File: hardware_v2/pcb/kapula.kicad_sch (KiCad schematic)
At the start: 166 parts, among them J1 Conn_02x10_Odd_Even, J2 Conn_02x10_Odd_Even, J3 U.FL, J4 U.FL, J5 U.FL, J6 U.FL, Q1 AO3401A, Q1 BSS84, Q2 AO3400A, Q3 AO3400A, Q4 AO3400A, Q5 AO3401A, T1 BW21S7511A01TF, T2 BW21S7511A01TF, T3 BW21S7511A01TF, T4 BW21S7511A01TF, U1 TP4054, U2 DW01+G, U3 XC6206P332MR, U4 FM8002A, U5 EFR32FG14P233F256GM48-B, U6 TG2016SMN 38.4000M-MCGNNM3, U7 XA213-G4J, Y1 32768 Hz

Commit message: PCB: Change some RF matching footprints, improve silkscreen
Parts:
- C74, C82: footprint kapula:C_0402_to_0603_HandSolder -> Capacitor_SMD:C_0603_1608Metric_Pad1.08x0.95mm_HandSolder; LCSC C1523 -> C1588
- L71, L72, L74, L75: footprint kapula:L_0402_to_0603_HandSolder -> Inductor_SMD:L_0402_1005Metric_Pad0.77x0.64mm_HandSolder
- R44, R45, R46, R47: footprint kapula:R_0402_to_0603_HandSolder -> Resistor_SMD:R_0603_1608Metric_Pad0.98x0.95mm_HandSolder
- R78: footprint kapula:R_0402_to_0603_HandSolder -> Resistor_SMD:R_0603_1608Metric_Pad0.98x0.95mm_HandSolder; LCSC C17168 -> C21189
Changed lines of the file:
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@@
       (effects (font (size 1.27 1.27)))
     )
-    (property "Footprint" "kapula:L_0402_to_0603_HandSolder" (at 177.8 196.85 0)
+    (property "Footprint" "Inductor_SMD:L_0402_1005Metric_Pad0.77x0.64mm_HandSolder" (at 177.8 196.85 0)
       (effects (font (size 1.27 1.27)) hide)
     )
@@
       (effects (font (size 1.27 1.27)))
     )
-    (property "Footprint" "kapula:C_0402_to_0603_HandSolder" (at 246.38 209.2452 0)
+    (property "Footprint" "Capacitor_SMD:C_0603_1608Metric_Pad1.08x0.95mm_HandSolder" (at 246.38 209.2452 0)
       (effects (font (size 1.27 1.27)) hide)
     )
@@
       (effects (font (size 1.27 1.27)) hide)
     )
-    (property "LCSC" "C1523" (at 250.19 208.28 0)
+    (property "LCSC" "C1588" (at 250.19 208.28 0)
       (effects (font (size 1.27 1.27)) hide)
     )
@@
       (effects (font (size 1.27 1.27)))
     )
-    (property "Footprint" "kapula:L_0402_to_0603_HandSolder" (at 177.8 207.01 0)
+    (property "Footprint" "Inductor_SMD:L_0402_1005Metric_Pad0.77x0.64mm_HandSolder" (at 177.8 207.01 0)
       (effects (font (size 1.27 1.27)) hide)
     )
@@
       (effects (font (size 1.27 1.27)))
     )
-    (property "Footprint" "kapula:C_0402_to_0603_HandSolder" (at 293.37 213.0552 0)
+    (property "Footprint" "Capacitor_SMD:C_0603_1608Metric_Pad1.08x0.95mm_HandSolder" (at 293.37 213.0552 0)
       (effects (font (size 1.27 1.27)) hide)
     )
@@
       (effects (font (size 1.27 1.27)) hide)
     )
-    (property "LCSC" "C1523" (at 297.18 212.09 0)
+    (property "LCSC" "C1588" (at 297.18 212.09 0)
       (effects (font (size 1.27 1.27)) hide)
     )
@@
       (effects (font (size 1.27 1.27)))
     )
-    (property "Footprint" "kapula:R_0402_to_0603_HandSolder" (at 393.7 25.908 90)
+    (property "Footprint" "Resistor_SMD:R_0603_1608Metric_Pad0.98x0.95mm_HandSolder" (at 393.7 25.908 90)
       (effects (font (size 1.27 1.27)) hide)
     )
@@
       (effects (font (size 1.27 1.27)))
     )
-    (property "Footprint" "kapula:L_0402_to_0603_HandSolder" (at 177.8 247.65 0)
+    (property "Footprint" "Inductor_SMD:L_0402_1005Metric_Pad0.77x0.64mm_HandSolder" (at 177.8 247.65 0)
       (effects (font (size 1.27 1.27)) hide)
     )
@@
       (effects (font (size 1.27 1.27)))
     )
-    (property "Footprint" "kapula:R_0402_to_0603_HandSolder" (at 336.55 210.312 90)
+    (property "Footprint" "Resistor_SMD:R_0603_1608Metric_Pad0.98x0.95mm_HandSolder" (at 336.55 210.312 90)
       (effects (font (size 1.27 1.27)) hide)
     )
@@
       (effects (font (size 1.27 1.27)) hide)
     )
-    (property "LCSC" "C17168" (at 336.55 212.09 0)
+    (property "LCSC" "C21189" (at 336.55 212.09 0)
       (effects (font (size 1.27 1.27)) hide)
     )
@@
       (effects (font (size 1.27 1.27)))
     )
-    (property "Footprint" "kapula:L_0402_to_0603_HandSolder" (at 177.8 229.87 0)
+    (property "Footprint" "Inductor_SMD:L_0402_1005Metric_Pad0.77x0.64mm_HandSolder" (at 177.8 229.87 0)
       (effects (font (size 1.27 1.27)) hide)
     )
@@
       (effects (font (size 1.27 1.27)))
     )
-    (property "Footprint" "kapula:R_0402_to_0603_HandSolder" (at 393.7 33.528 90)
+    (property "Footprint" "Resistor_SMD:R_0603_1608Metric_Pad0.98x0.95mm_HandSolder" (at 393.7 33.528 90)
       (effects (font (size 1.27 1.27)) hide)
     )
@@
       (effects (font (size 1.27 1.27)))
     )
-    (property "Footprint" "kapula:R_0402_to_0603_HandSolder" (at 393.7 30.988 90)
+    (property "Footprint" "Resistor_SMD:R_0603_1608Metric_Pad0.98x0.95mm_HandSolder" (at 393.7 30.988 90)
       (effects (font (size 1.27 1.27)) hide)
     )
@@
       (effects (font (size 1.27 1.27)))
     )
-    (property "Footprint" "kapula:R_0402_to_0603_HandSolder" (at 393.7 28.448 90)
+    (property "Footprint" "Resistor_SMD:R_0603_1608Metric_Pad0.98x0.95mm_HandSolder" (at 393.7 28.448 90)
       (effects (font (size 1.27 1.27)) hide)
     )

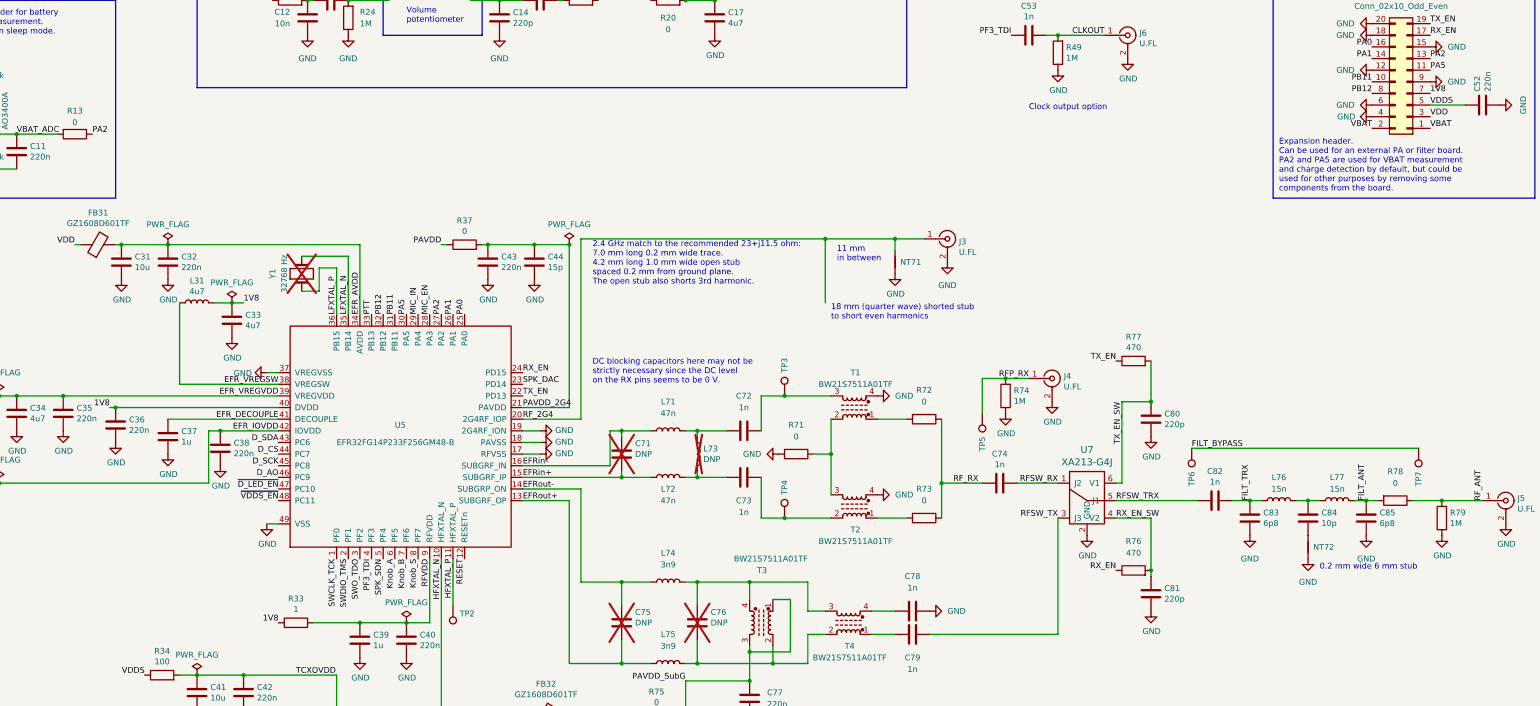
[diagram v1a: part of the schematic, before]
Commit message: PCB: Rename net 1V8 to DVDD
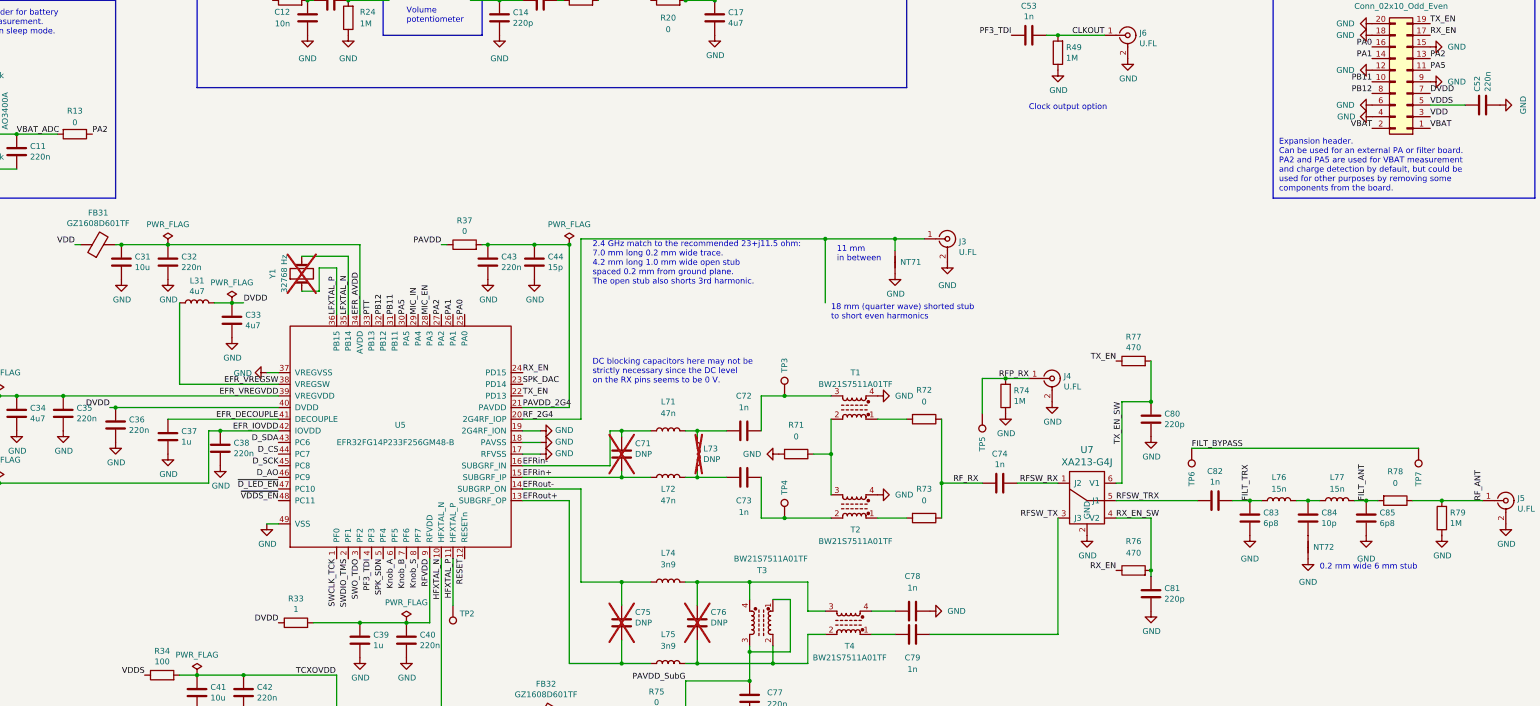
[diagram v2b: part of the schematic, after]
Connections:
- net 1V8 renamed DVDD
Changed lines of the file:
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@@
     (effects (font (size 1.27 1.27)) (justify right bottom))
   )
-  (label "1V8" (at 344.17 123.19 0) (fields_autoplaced)
+  (label "DVDD" (at 344.17 123.19 0) (fields_autoplaced)
     (effects (font (size 1.27 1.27)) (justify left bottom))
   )
@@
     (effects (font (size 1.27 1.27)) (justify left bottom))
   )
-  (label "1V8" (at 55.88 191.77 180) (fields_autoplaced)
+  (label "DVDD" (at 55.88 191.77 180) (fields_autoplaced)
     (effects (font (size 1.27 1.27)) (justify right bottom))
   )
@@
     (effects (font (size 1.27 1.27)) (justify right bottom))
   )
-  (label "1V8" (at 85.09 168.91 0) (fields_autoplaced)
+  (label "DVDD" (at 85.09 168.91 0) (fields_autoplaced)
     (effects (font (size 1.27 1.27)) (justify left bottom))
   )
@@
     (effects (font (size 1.27 1.27)) (justify right bottom))
   )
-  (label "1V8" (at 92.71 238.76 180) (fields_autoplaced)
-    (effects (font (size 1.27 1.27)) (justify right bottom))
-  )
+  (label "DVDD" (at 92.71 238.76 180) (fields_autoplaced)
+    (effects (font (size 1.27 1.27)) (justify right bottom))
+  )
